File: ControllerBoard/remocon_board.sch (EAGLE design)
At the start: 61 parts, among them CN1 POWER_IF, CN2 PICkit_IF, CN3 ROTARY_ENCODER, CN4 FEEDER_IF, CN5 UART_IF, CN6 POWER_IF_FOR_ESP, Q1 2SC1815, Q3 2SC1815, Q4 2SK2232, SW1 10-XX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

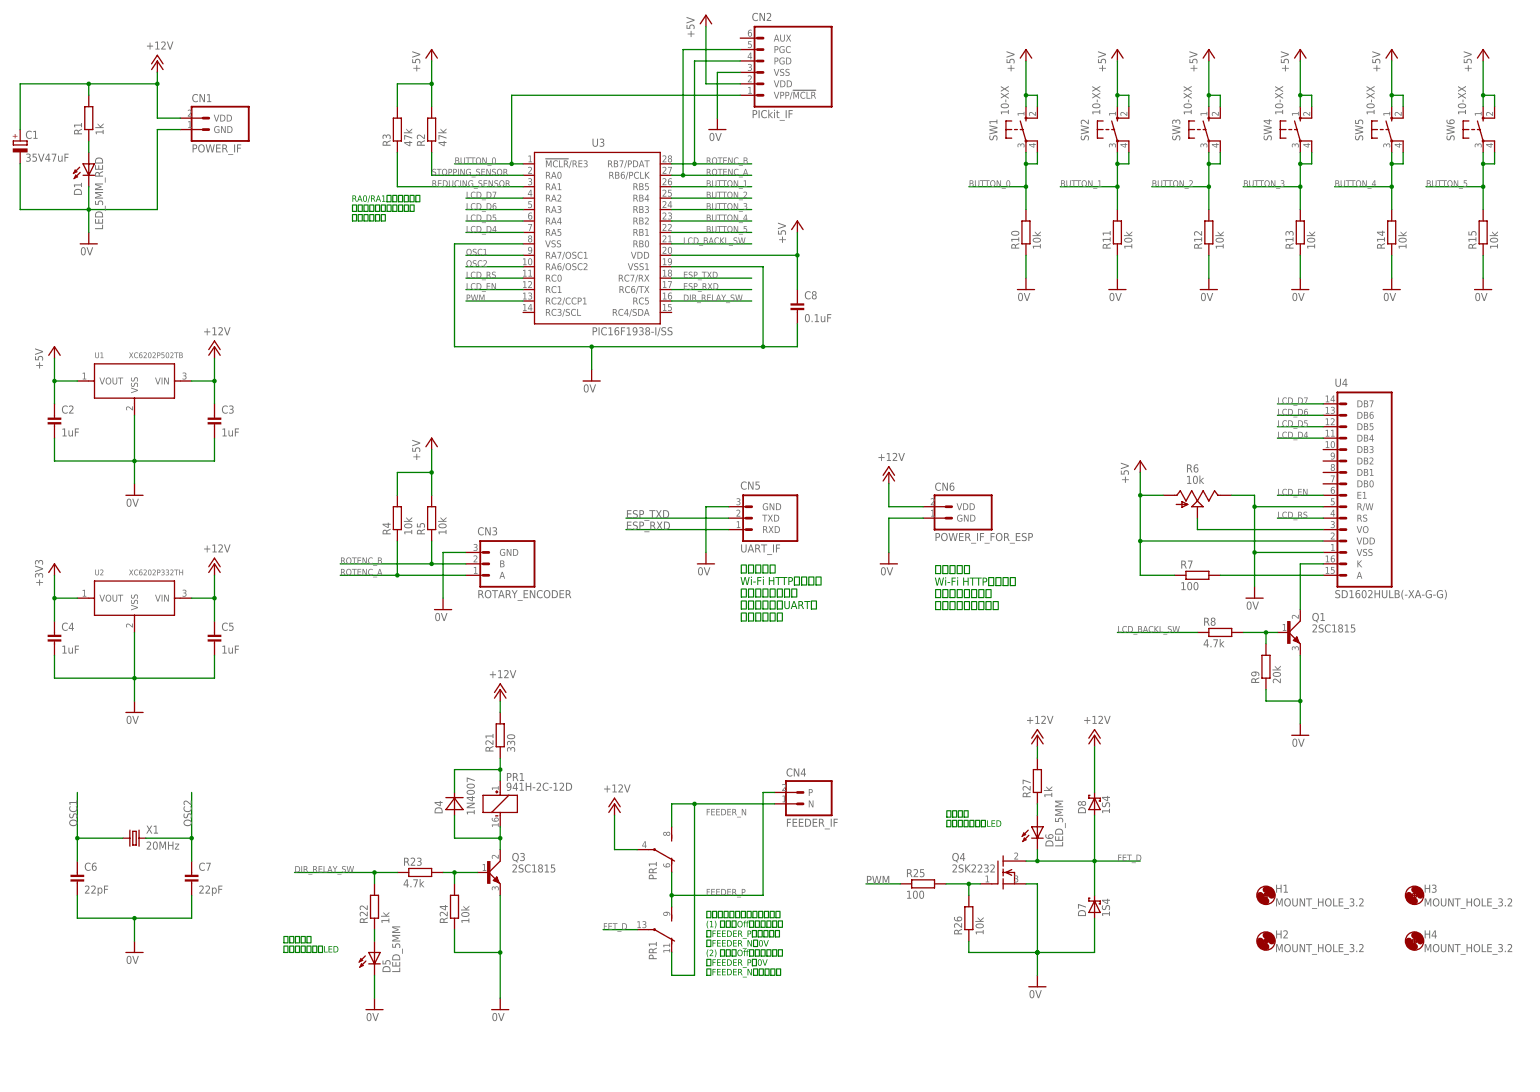
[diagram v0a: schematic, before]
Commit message: MODE_SELECT端子を新設
・PICのファームウェアを共通化する目的
・MODE_SELECT=LOWの場合は親機（パワーコントローラー部）
・MODE_SELECT=HIGHの場合は子機（リモコン部）
・ディレクトリー名を EAGLE —> ControllerBoardに改称
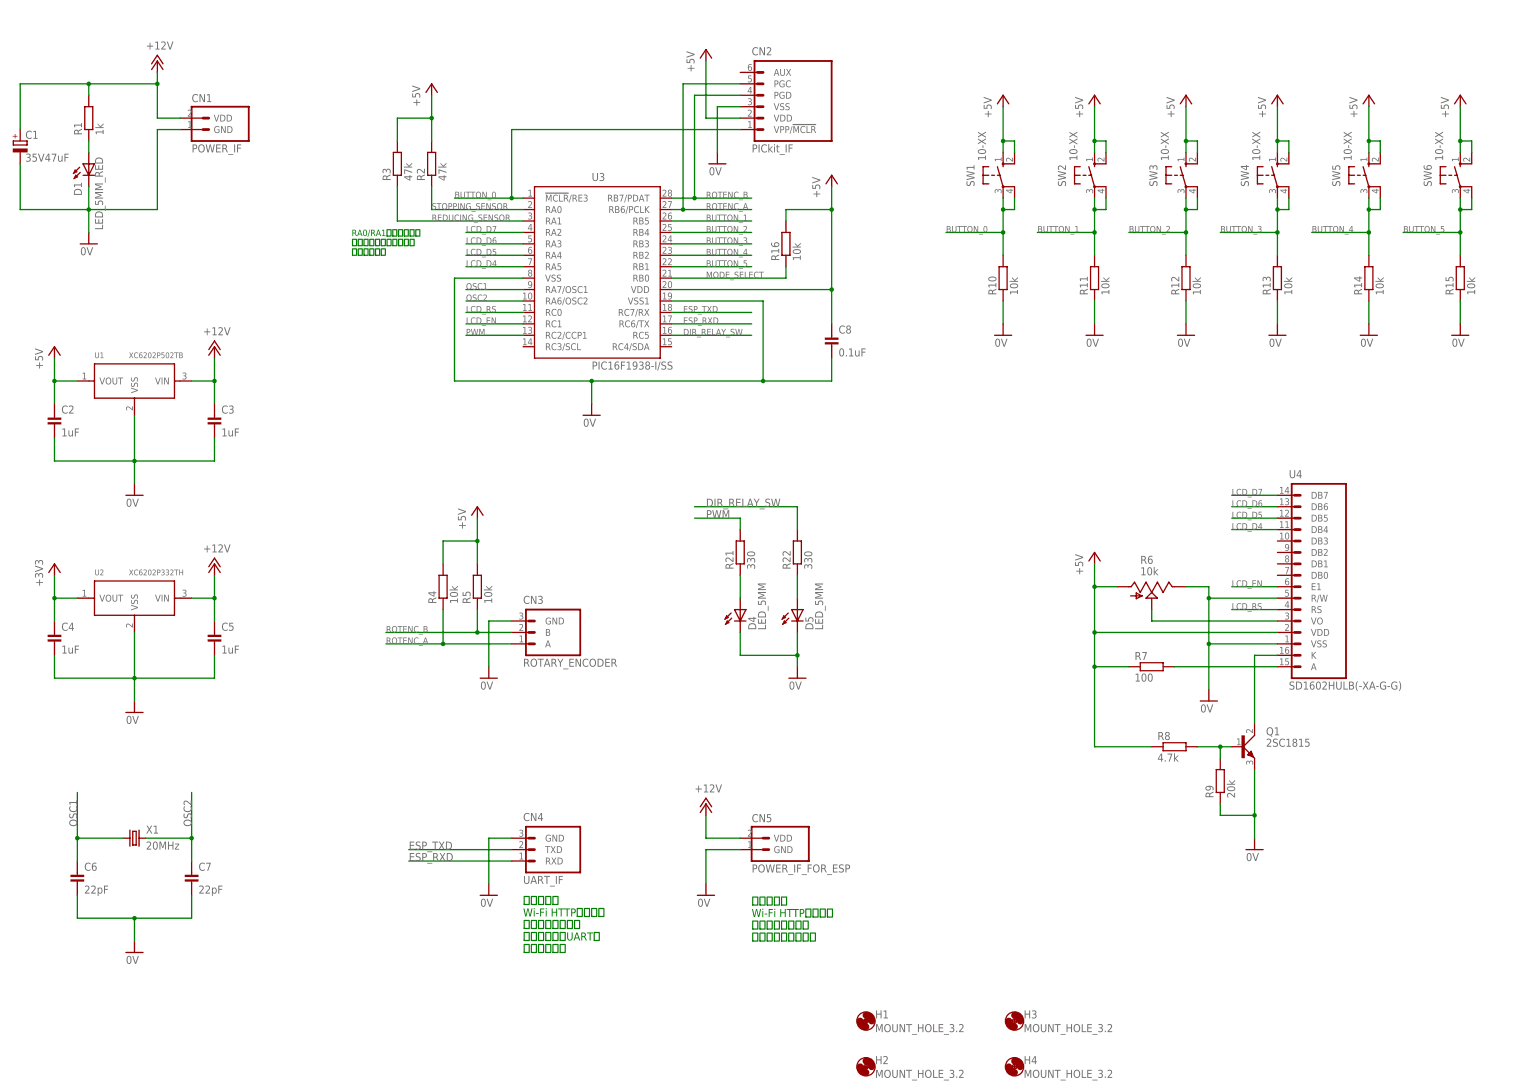
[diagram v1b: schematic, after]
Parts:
- removed CN6: POWER_IF_FOR_ESP, PartsForProto:POWER_IF
- removed D6: LED_5MM, Parts:LED_5MM
- removed D7, D8: 1S4, Parts:1S4
- removed PR1: 941H-2C-12D, Parts:941H-2C-12D
- removed Q3: 2SC1815, Parts:2SC1815
- removed Q4: 2SK2232, Parts:2SK2232
- removed R23: 4.7k, Parts:RESISTOR_300MIL
- removed R24, R26: 10k, Parts:RESISTOR_300MIL
- removed R25: 100, Parts:RESISTOR_300MIL
- removed R27: 1k, Parts:RESISTOR_300MIL
- added R16: 10k, Parts:RESISTOR_300MIL
- CN4: value FEEDER_IF -> UART_IF; device PartsForProto:FEEDER_IF -> PartsForProto:UART_IF
- CN5: value UART_IF -> POWER_IF_FOR_ESP; device PartsForProto:UART_IF -> PartsForProto:POWER_IF
- D4: value 1N4007 -> LED_5MM; device Parts:1N4007 -> Parts:LED_5MM
- R22: value 1k -> 330
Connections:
- removed net +3V3: C4.1, U2.VOUT
- removed net FEEDER_N: CN4.N, PR12.S, PR13.O
- removed net FEEDER_P: CN4.P, PR12.O, PR13.S
- removed net FET_D: D6.C, D7.C, D8.A, PR13.P, Q4.D
- removed net LCD_BACKL_SW: R8.1, U3.RB0
- removed net N$13: D4.C, PR11.+, R21.1
- removed net N$14: Q3.B, R23.2, R24.2
- removed net N$15: D4.A, PR11.-, Q3.C
- removed net N$3 (its old number): Q4.G, R25.2, R26.2
- new net MODE_SELECT: R16.1, U3.RB0
- net +12V: now also CN5.VDD; no longer CN6.VDD, D8.C, PR12.P, R21.2, R27.2
- net +5V: now also C4.1, R16.2, R8.1, U2.VOUT
- net 0V: now also CN4.GND, D4.C; no longer CN6.GND, D7.A, Q3.E, Q4.S, R24.1, R26.1
- net DIR_RELAY_SW: no longer R23.1
- net ESP_RXD: now also CN4.RXD; no longer CN5.RXD
- net ESP_TXD: now also CN4.TXD; no longer CN5.TXD
- net N$8: now also D4.A, R21.1; no longer D6.A, R27.1
- net PWM: now also R21.2; no longer R25.1
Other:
- note added: "別途作成の Wi-Fi HTTP通信基板 （子機モード）の ソフトウェアUARTに 接続します。"
- note added: "別途作成の Wi-Fi HTTP通信基板 （子機モード）へ 電源を供給します。"
- note removed: "フィーダーの正転／逆転制御 (1) リレーOff時（正転時） FEEDER_P：駆動電圧 FEEDER_N：0V (2) リレーOff時（逆転時） FEEDER_P：0V FEEDER_N：駆動電圧"
- note removed: "供給電圧 インジケーターLED"
- note removed: "別途作成の Wi-Fi HTTP通信基板 （親機モード）の ソフトウェアUARTに 接続します。"
- note removed: "別途作成の Wi-Fi HTTP通信基板 （親機モード）へ 電源を供給します。"
- note removed: "正転／逆転 インジケーターLED"
- moved on the sheet: C8, CN2, CN3, D5, H1, H2, H3, H4, Q1, R10, R11, R12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
